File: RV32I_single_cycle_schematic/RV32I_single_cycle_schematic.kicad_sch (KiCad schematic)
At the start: 14 parts, among them U1 PC_src, U10 alu_a, U11 alu_b, U12 ALU_Control, U13 Data_Memory, U14 WB_mux, U2 Program_Counter, U3 PCplus4, U4 Instr_Mem, U5 Instr_Decoder, U6 Register_file, U7 ALU, U8 Branch_Control, U9 Immediate_Generator

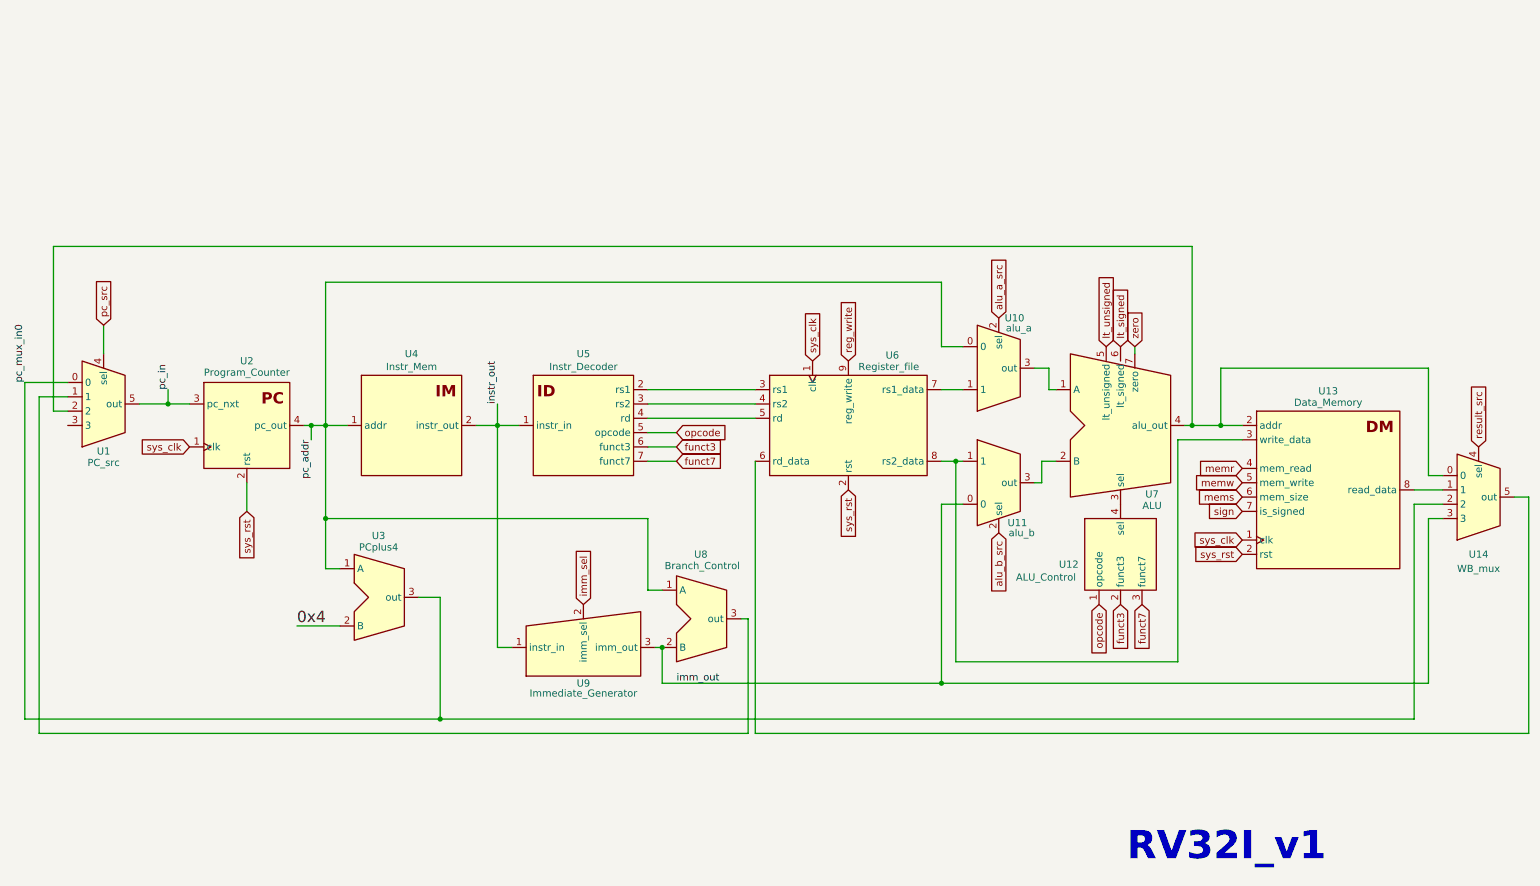
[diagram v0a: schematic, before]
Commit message: updated RV32I schematic
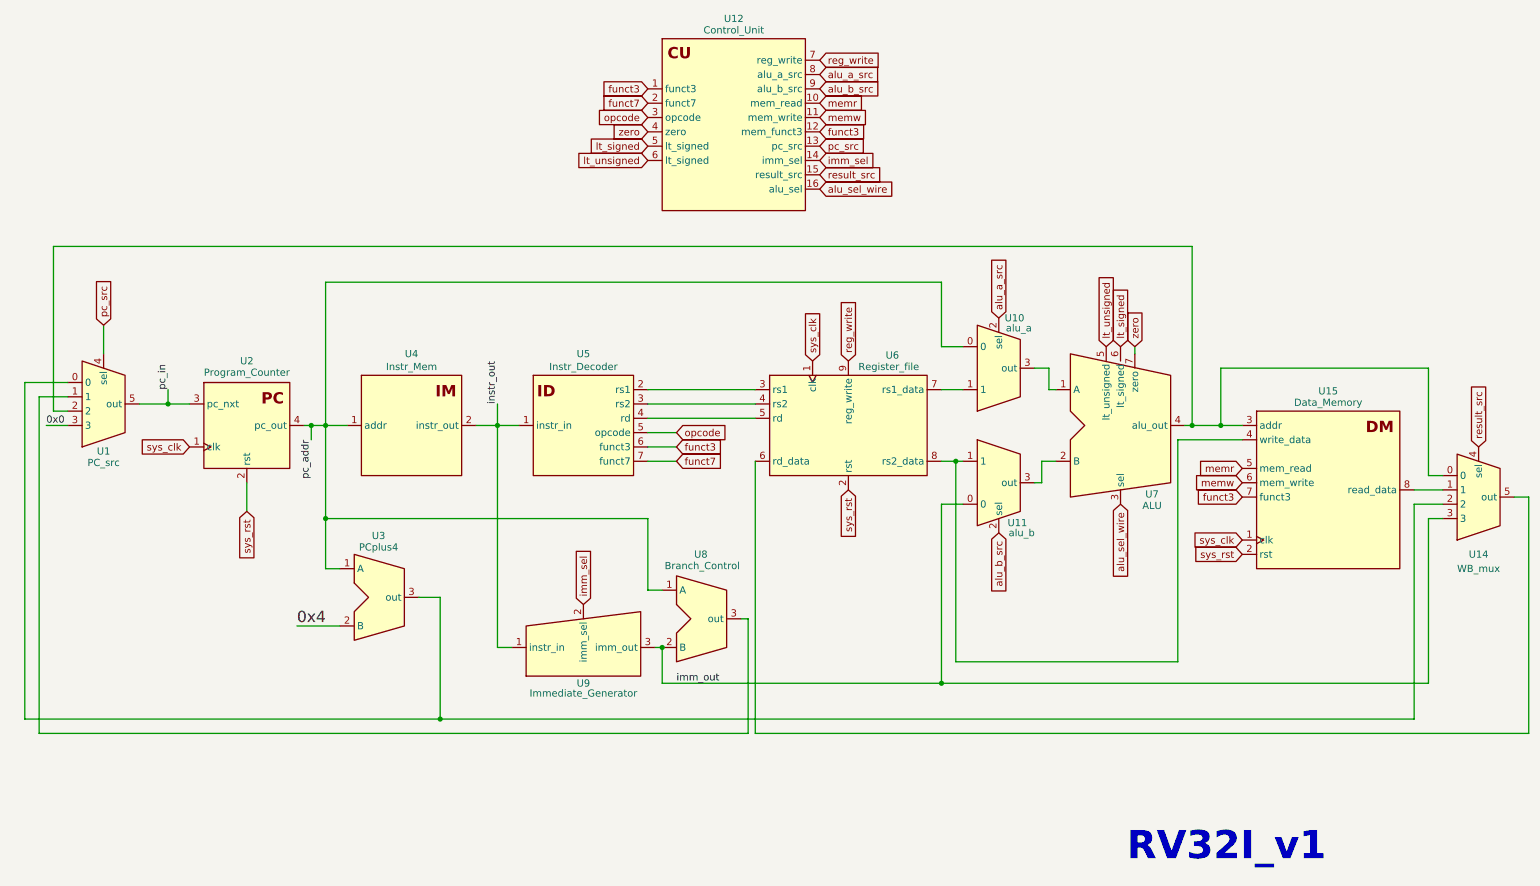
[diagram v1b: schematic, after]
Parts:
- removed U12: ALU_Control, symbol DIGITAL_BLOCKS:alu_control
- removed U13: Data_Memory, symbol DIGITAL_BLOCKS:Data_Memory
- added U12: Control_Unit, symbol DIGITAL_BLOCKS:Control_Unit
- added U15: Data_Memory, symbol DIGITAL_BLOCKS:Data_Memory
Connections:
- net alu_a_src: now also U12.8 (alu_a_src)
- net alu_b_src: now also U12.9 (alu_b_src)
- net funct3: now also U12.1 (funct3), U12.12 (mem_funct3), U15.7 (funct3)
- net funct7: now also U12.2 (funct7)
- net imm_sel: now also U12.14 (imm_sel)
- net lt_signed: now also U12.5 (lt_signed)
- net lt_unsigned: now also U12.6 (lt_signed)
- net memr: now also U12.10 (mem_read), U15.5 (mem_read)
- net memw: now also U12.11 (mem_write), U15.6 (mem_write)
- net opcode: now also U12.3 (opcode)
- net pc_src: now also U12.13 (pc_src)
- net reg_write: now also U12.7 (reg_write)
- net result_src: now also U12.15 (result_src)
- net sys_clk: now also U15.1 (clk)
- net sys_rst: now also U15.2 (rst)
- net zero: now also U12.4 (zero)
- net alu_sel_wire: now reaches U7.3 (sel)
- net alu_sel_wire: now also U12.16 (alu_sel)
- net at U1.2, U14.0, U7.4 (alu_out): now also U15.3 (addr)
- net at U11.1, U6.8 (rs2_data): now also U15.4 (write_data)
- net at U14.1: now also U15.8 (read_data)
- net 0x0: now reaches U1.3
- net pc_mux_in0: no longer names the net of U1.0, U14.2, U3.3 (out)
